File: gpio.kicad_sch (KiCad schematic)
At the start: 4 parts

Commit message: write some things down
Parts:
- U1: renamed from U?; value MCIMX6YxxVMxxxx -> MCIMX6Y2DVM09AB; Manufacturer (none) -> NXP; MfgPartNo (none) -> MCIMX6Y2DVM09AB; Vendor (none) -> Digi-Key; VendorPartNo (none) -> 568-14995-ND
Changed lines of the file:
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@@
   (symbol (lib_id "catfood:MCIMX6YxxVMxxxx") (at 149.86 59.69 0) (unit 11)
     (in_bom yes) (on_board yes) (fields_autoplaced)
-    (property "Reference" "U?" (id 0) (at 149.86 27.94 0))
-    (property "Value" "MCIMX6YxxVMxxxx" (id 1) (at 149.86 30.48 0))
+    (property "Reference" "U1" (id 0) (at 149.86 27.94 0))
+    (property "Value" "MCIMX6Y2DVM09AB" (id 1) (at 149.86 30.48 0))
     (property "Footprint" "" (id 2) (at 139.7 40.64 0)
       (effects (font (size 1.27 1.27)) hide)
     )
     (property "Datasheet" "" (id 3) (at 139.7 40.64 0)
+      (effects (font (size 1.27 1.27)) hide)
+    )
+    (property "Manufacturer" "NXP" (id 4) (at 149.86 38.1 0)
+      (effects (font (size 1.27 1.27)) hide)
+    )
+    (property "MfgPartNo" "MCIMX6Y2DVM09AB" (id 5) (at 149.86 40.64 0)
+      (effects (font (size 1.27 1.27)) hide)
+    )
+    (property "Vendor" "Digi-Key" (id 6) (at 149.86 43.18 0)
+      (effects (font (size 1.27 1.27)) hide)
+    )
+    (property "VendorPartNo" "568-14995-ND" (id 7) (at 149.86 45.72 0)
       (effects (font (size 1.27 1.27)) hide)
     )
@@
   (symbol (lib_id "catfood:MCIMX6YxxVMxxxx") (at 105.41 62.23 0) (unit 5)
     (in_bom yes) (on_board yes) (fields_autoplaced)
-    (property "Reference" "U?" (id 0) (at 105.41 30.48 0))
-    (property "Value" "MCIMX6YxxVMxxxx" (id 1) (at 105.41 33.02 0))
+    (property "Reference" "U1" (id 0) (at 105.41 30.48 0))
+    (property "Value" "MCIMX6Y2DVM09AB" (id 1) (at 105.41 33.02 0))
     (property "Footprint" "" (id 2) (at 95.25 43.18 0)
       (effects (font (size 1.27 1.27)) hide)
     )
     (property "Datasheet" "" (id 3) (at 95.25 43.18 0)
+      (effects (font (size 1.27 1.27)) hide)
+    )
+    (property "Manufacturer" "NXP" (id 4) (at 105.41 40.64 0)
+      (effects (font (size 1.27 1.27)) hide)
+    )
+    (property "MfgPartNo" "MCIMX6Y2DVM09AB" (id 5) (at 105.41 43.18 0)
+      (effects (font (size 1.27 1.27)) hide)
+    )
+    (property "Vendor" "Digi-Key" (id 6) (at 105.41 45.72 0)
+      (effects (font (size 1.27 1.27)) hide)
+    )
+    (property "VendorPartNo" "568-14995-ND" (id 7) (at 105.41 48.26 0)
       (effects (font (size 1.27 1.27)) hide)
     )
@@
   (symbol (lib_id "catfood:MCIMX6YxxVMxxxx") (at 54.61 59.69 0) (unit 4)
     (in_bom yes) (on_board yes) (fields_autoplaced)
-    (property "Reference" "U?" (id 0) (at 54.61 27.94 0))
-    (property "Value" "MCIMX6YxxVMxxxx" (id 1) (at 54.61 30.48 0))
+    (property "Reference" "U1" (id 0) (at 54.61 27.94 0))
+    (property "Value" "MCIMX6Y2DVM09AB" (id 1) (at 54.61 30.48 0))
     (property "Footprint" "" (id 2) (at 44.45 40.64 0)
       (effects (font (size 1.27 1.27)) hide)
     )
     (property "Datasheet" "" (id 3) (at 44.45 40.64 0)
+      (effects (font (size 1.27 1.27)) hide)
+    )
+    (property "Manufacturer" "NXP" (id 4) (at 54.61 38.1 0)
+      (effects (font (size 1.27 1.27)) hide)
+    )
+    (property "MfgPartNo" "MCIMX6Y2DVM09AB" (id 5) (at 54.61 40.64 0)
+      (effects (font (size 1.27 1.27)) hide)
+    )
+    (property "Vendor" "Digi-Key" (id 6) (at 54.61 43.18 0)
+      (effects (font (size 1.27 1.27)) hide)
+    )
+    (property "VendorPartNo" "568-14995-ND" (id 7) (at 54.61 45.72 0)
       (effects (font (size 1.27 1.27)) hide)
     )
@@
   (symbol (lib_id "catfood:MCIMX6YxxVMxxxx") (at 109.22 107.95 0) (unit 7)
     (in_bom yes) (on_board yes) (fields_autoplaced)
-    (property "Reference" "U?" (id 0) (at 120.65 85.7249 0)
+    (property "Reference" "U1" (id 0) (at 120.65 85.7249 0)
       (effects (font (size 1.27 1.27)) (justify left))
     )
-    (property "Value" "MCIMX6YxxVMxxxx" (id 1) (at 120.65 88.2649 0)
+    (property "Value" "MCIMX6Y2DVM09AB" (id 1) (at 120.65 88.2649 0)
       (effects (font (size 1.27 1.27)) (justify left))
     )
@@
       (effects (font (size 1.27 1.27)) hide)
     )
+    (property "Manufacturer" "NXP" (id 4) (at 120.65 95.8849 0)
+      (effects (font (size 1.27 1.27)) (justify left) hide)
+    )
+    (property "MfgPartNo" "MCIMX6Y2DVM09AB" (id 5) (at 120.65 98.4249 0)
+      (effects (font (size 1.27 1.27)) (justify left) hide)
+    )
+    (property "Vendor" "Digi-Key" (id 6) (at 120.65 100.9649 0)
+      (effects (font (size 1.27 1.27)) (justify left) hide)
+    )
+    (property "VendorPartNo" "568-14995-ND" (id 7) (at 120.65 103.5049 0)
+      (effects (font (size 1.27 1.27)) (justify left) hide)
+    )
     (pin "A1")

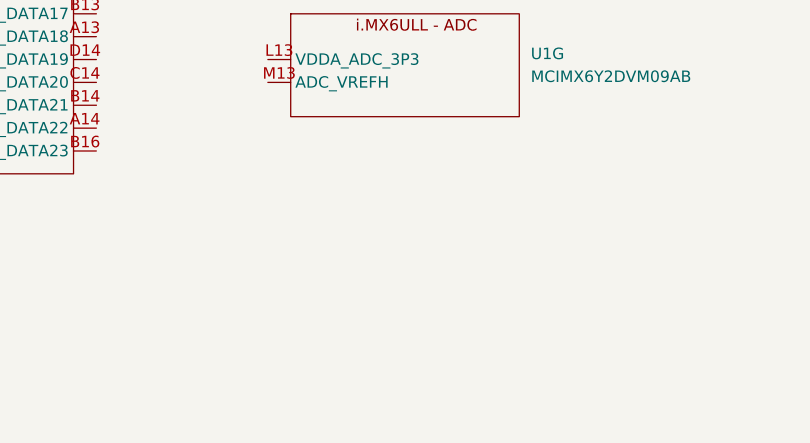
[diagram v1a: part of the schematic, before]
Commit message: Remove WiFi
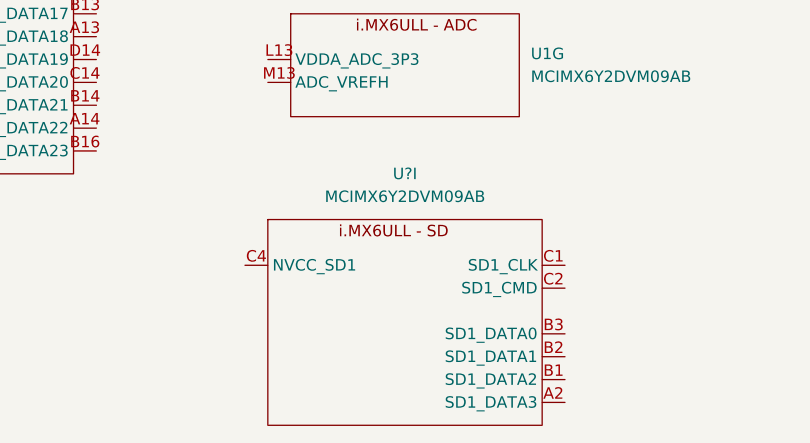
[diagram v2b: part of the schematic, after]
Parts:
- added U?: MCIMX6Y2DVM09AB, symbol catfood:MCIMX6YxxVMxxxx

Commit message: USB, GPIO
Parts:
- added C?: 1uF 0402, symbol Device:C_Small
- added C? (x5): 0.22uF 0402, symbol Device:C_Small
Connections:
- net VDD_3V3: now reaches U1.J13 (NVCC_GPIO)
- net VDD_3V3: now also U1.E13 (NVCC_LCD), U1.F4 (NVCC_CSI), U1.L13 (VDDA_ADC_3P3), U1.M13 (ADC_VREFH), U?.C4 (NVCC_SD1), C?.1, C?.1, C?.1, C?.1, C?.1, C?.1
- net ENET_MDIO: now reaches U1.K17 (GPIO1_IO06)
- net ENET_MDC: now reaches U1.L16 (GPOI1_IO07)
- net ~{ENET1_RST}: now reaches U1.N17 (GPIO1_IO08)
- new net GND: C?.2, C?.2, C?.2, C?.2, C?.2, C?.2
- no-connect marks 0 -> 54
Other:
- moved on the sheet: U1E, U1G, U1K, U?I

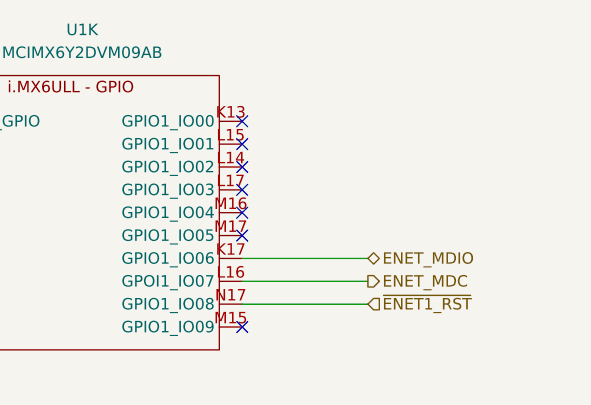
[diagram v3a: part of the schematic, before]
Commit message: USB host port capacitance, load switch
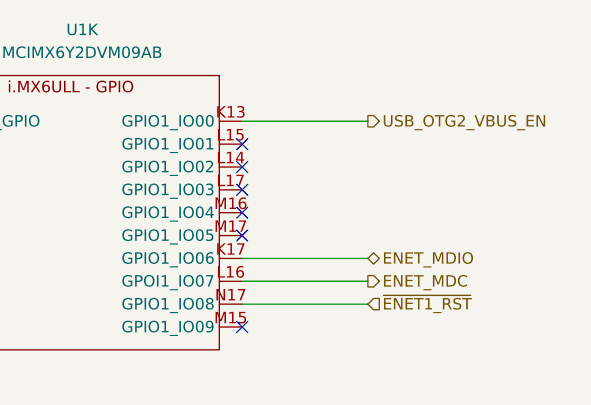
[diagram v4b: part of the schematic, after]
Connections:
- net USB_OTG2_VBUS_EN: now reaches U1.K13 (GPIO1_IO00)
- no-connect marks 54 -> 53
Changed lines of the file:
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@@
   (no_connect (at 72.39 45.72))
   (no_connect (at 78.105 155.575))
-  (no_connect (at 223.52 36.83))
   (no_connect (at 78.105 168.275))
   (no_connect (at 36.83 49.53))
@@
   )
   (wire (pts (xy 136.525 93.98) (xy 136.525 92.71))
+    (stroke (width 0) (type default) (color 0 0 0 0))
+  )
+  (wire (pts (xy 223.52 36.83) (xy 237.49 36.83))
     (stroke (width 0) (type default) (color 0 0 0 0))
   )
@@
     (effects (font (size 1.27 1.27)) (justify left))
   )
+  (hierarchical_label "USB_OTG2_VBUS_EN" (shape output) (at 237.49 36.83 0)
+    (effects (font (size 1.27 1.27)) (justify left))
+  )

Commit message: Annotation
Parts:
- gave numbers to parts that had none: 7
- renumbered U1 to U4
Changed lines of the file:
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@@
   (symbol (lib_id "catfood:VDD_3V3") (at 24.13 137.795 0) (unit 1)
     (in_bom yes) (on_board yes) (fields_autoplaced)
-    (property "Reference" "#PWR?" (id 0) (at 24.13 141.605 0)
+    (property "Reference" "#PWR0109" (id 0) (at 24.13 141.605 0)
       (effects (font (size 1.27 1.27)) hide)
     )
@@
   (symbol (lib_id "Device:C_Small") (at 136.525 96.52 0) (unit 1)
     (in_bom yes) (on_board yes) (fields_autoplaced)
-    (property "Reference" "C?" (id 0) (at 139.7 95.2562 0)
+    (property "Reference" "C88" (id 0) (at 139.7 95.2562 0)
       (effects (font (size 1.27 1.27)) (justify left))
     )
@@
   (symbol (lib_id "power:GND") (at 153.67 104.14 0) (unit 1)
     (in_bom yes) (on_board yes) (fields_autoplaced)
-    (property "Reference" "#PWR?" (id 0) (at 153.67 110.49 0)
+    (property "Reference" "#PWR0112" (id 0) (at 153.67 110.49 0)
       (effects (font (size 1.27 1.27)) hide)
     )
@@
   (symbol (lib_id "catfood:MCIMX6YxxVMxxxx") (at 205.74 58.42 0) (unit 11)
     (in_bom yes) (on_board yes) (fields_autoplaced)
-    (property "Reference" "U1" (id 0) (at 205.74 26.67 0))
+    (property "Reference" "U4" (id 0) (at 205.74 26.67 0))
     (property "Value" "MCIMX6Y2DVM09AB" (id 1) (at 205.74 29.21 0))
     (property "Footprint" "" (id 2) (at 195.58 39.37 0)
@@
   (symbol (lib_id "catfood:MCIMX6YxxVMxxxx") (at 200.025 158.115 0) (unit 9)
     (in_bom yes) (on_board yes) (fields_autoplaced)
-    (property "Reference" "U?" (id 0) (at 200.025 126.365 0))
+    (property "Reference" "U4" (id 0) (at 200.025 126.365 0))
     (property "Value" "MCIMX6Y2DVM09AB" (id 1) (at 200.025 128.905 0))
     (property "Footprint" "" (id 2) (at 189.865 139.065 0)
@@
   (symbol (lib_id "Device:C_Small") (at 19.05 42.545 0) (unit 1)
     (in_bom yes) (on_board yes) (fields_autoplaced)
-    (property "Reference" "C?" (id 0) (at 21.59 41.2812 0)
+    (property "Reference" "C86" (id 0) (at 21.59 41.2812 0)
       (effects (font (size 1.27 1.27)) (justify left))
     )
@@
   (symbol (lib_id "catfood:MCIMX6YxxVMxxxx") (at 60.325 161.925 0) (unit 5)
     (in_bom yes) (on_board yes) (fields_autoplaced)
-    (property "Reference" "U1" (id 0) (at 60.325 130.175 0))
+    (property "Reference" "U4" (id 0) (at 60.325 130.175 0))
     (property "Value" "MCIMX6Y2DVM09AB" (id 1) (at 60.325 132.715 0))
     (property "Footprint" "" (id 2) (at 50.165 142.875 0)
@@
   (symbol (lib_id "power:GND") (at 19.05 50.165 0) (unit 1)
     (in_bom yes) (on_board yes) (fields_autoplaced)
-    (property "Reference" "#PWR?" (id 0) (at 19.05 56.515 0)
+    (property "Reference" "#PWR0108" (id 0) (at 19.05 56.515 0)
       (effects (font (size 1.27 1.27)) hide)
     )
@@
   (symbol (lib_id "catfood:VDD_3V3") (at 153.67 89.535 0) (unit 1)
     (in_bom yes) (on_board yes) (fields_autoplaced)
-    (property "Reference" "#PWR?" (id 0) (at 153.67 93.345 0)
+    (property "Reference" "#PWR0111" (id 0) (at 153.67 93.345 0)
       (effects (font (size 1.27 1.27)) hide)
     )
@@
   (symbol (lib_id "power:GND") (at 168.91 49.53 0) (unit 1)
     (in_bom yes) (on_board yes) (fields_autoplaced)
-    (property "Reference" "#PWR?" (id 0) (at 168.91 55.88 0)
+    (property "Reference" "#PWR0116" (id 0) (at 168.91 55.88 0)
       (effects (font (size 1.27 1.27)) hide)
     )
@@
   (symbol (lib_id "Device:C_Small") (at 153.67 96.52 0) (unit 1)
     (in_bom yes) (on_board yes) (fields_autoplaced)
-    (property "Reference" "C?" (id 0) (at 156.21 95.2562 0)
+    (property "Reference" "C89" (id 0) (at 156.21 95.2562 0)
       (effects (font (size 1.27 1.27)) (justify left))
     )
@@
   (symbol (lib_id "Device:C_Small") (at 24.13 144.78 0) (unit 1)
     (in_bom yes) (on_board yes) (fields_autoplaced)
-    (property "Reference" "C?" (id 0) (at 26.67 143.5162 0)
+    (property "Reference" "C87" (id 0) (at 26.67 143.5162 0)
       (effects (font (size 1.27 1.27)) (justify left))
     )
@@
   (symbol (lib_id "catfood:MCIMX6YxxVMxxxx") (at 54.61 59.69 0) (unit 4)
     (in_bom yes) (on_board yes) (fields_autoplaced)
-    (property "Reference" "U1" (id 0) (at 54.61 27.94 0))
+    (property "Reference" "U4" (id 0) (at 54.61 27.94 0))
     (property "Value" "MCIMX6Y2DVM09AB" (id 1) (at 54.61 30.48 0))
     (property "Footprint" "" (id 2) (at 44.45 40.64 0)
@@
   (symbol (lib_id "power:GND") (at 24.13 152.4 0) (unit 1)
     (in_bom yes) (on_board yes) (fields_autoplaced)
-    (property "Reference" "#PWR?" (id 0) (at 24.13 158.75 0)
+    (property "Reference" "#PWR0110" (id 0) (at 24.13 158.75 0)
       (effects (font (size 1.27 1.27)) hide)
     )
@@
   (symbol (lib_id "catfood:MCIMX6YxxVMxxxx") (at 193.04 114.3 0) (unit 7)
     (in_bom yes) (on_board yes) (fields_autoplaced)
-    (property "Reference" "U1" (id 0) (at 204.47 92.0749 0)
+    (property "Reference" "U4" (id 0) (at 204.47 92.0749 0)
       (effects (font (size 1.27 1.27)) (justify left))
     )
@@
   (symbol (lib_id "power:GND") (at 163.83 147.955 0) (unit 1)
     (in_bom yes) (on_board yes) (fields_autoplaced)
-    (property "Reference" "#PWR?" (id 0) (at 163.83 154.305 0)
+    (property "Reference" "#PWR0114" (id 0) (at 163.83 154.305 0)
       (effects (font (size 1.27 1.27)) hide)
     )
@@
   (symbol (lib_id "catfood:VDD_3V3") (at 163.83 133.35 0) (unit 1)
     (in_bom yes) (on_board yes) (fields_autoplaced)
-    (property "Reference" "#PWR?" (id 0) (at 163.83 137.16 0)
+    (property "Reference" "#PWR0113" (id 0) (at 163.83 137.16 0)
       (effects (font (size 1.27 1.27)) hide)
     )
@@
   (symbol (lib_id "Device:C_Small") (at 168.91 41.91 0) (unit 1)
     (in_bom yes) (on_board yes) (fields_autoplaced)
-    (property "Reference" "C?" (id 0) (at 171.45 40.6462 0)
+    (property "Reference" "C91" (id 0) (at 171.45 40.6462 0)
       (effects (font (size 1.27 1.27)) (justify left))
     )
@@
   (symbol (lib_id "catfood:VDD_3V3") (at 168.91 34.925 0) (unit 1)
     (in_bom yes) (on_board yes) (fields_autoplaced)
-    (property "Reference" "#PWR?" (id 0) (at 168.91 38.735 0)
+    (property "Reference" "#PWR0115" (id 0) (at 168.91 38.735 0)
       (effects (font (size 1.27 1.27)) hide)
     )
@@
   (symbol (lib_id "Device:C_Small") (at 163.83 140.335 0) (unit 1)
     (in_bom yes) (on_board yes) (fields_autoplaced)
-    (property "Reference" "C?" (id 0) (at 166.37 139.0712 0)
+    (property "Reference" "C90" (id 0) (at 166.37 139.0712 0)
       (effects (font (size 1.27 1.27)) (justify left))
     )
@@
   (symbol (lib_id "catfood:VDD_3V3") (at 19.05 35.56 0) (unit 1)
     (in_bom yes) (on_board yes) (fields_autoplaced)
-    (property "Reference" "#PWR?" (id 0) (at 19.05 39.37 0)
-      (effects (font (size 1.27 1.27)) hide)
-    )
+    (property "Reference" "#PWR0107" (id 0) (at 19.05 39.37 0)
+      (effects (font (size 1.27 1.27)) hide)
+    )
